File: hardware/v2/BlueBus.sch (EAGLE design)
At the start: 139 parts, among them J1 3PIN_953442_1, J2 6PIN_953442_1, J3 6PIN_5_103166_1, J4 SJ2-35853A-SMT-TR, J5 SMB_CONN, J6 USB3080-30-01-A, J7 PCM12SMTR, J8 TC2030NL, Q1 NMOSFET-BSS138K, Q2 NMOSFET-BSS138K, Q3 PMOSFET-DMP32D4SSOT323, U1 MPQ4420, U10 PCM5122, U11 PAM8406, U2 TH3122.4, U3 FT231XS, U4 S-1212BC0-U5T1U, U5 XC6210, U6 CAT25M01, U7 PIC24FJ1024GA606, U8 BM83SM1, U9 DIT4096

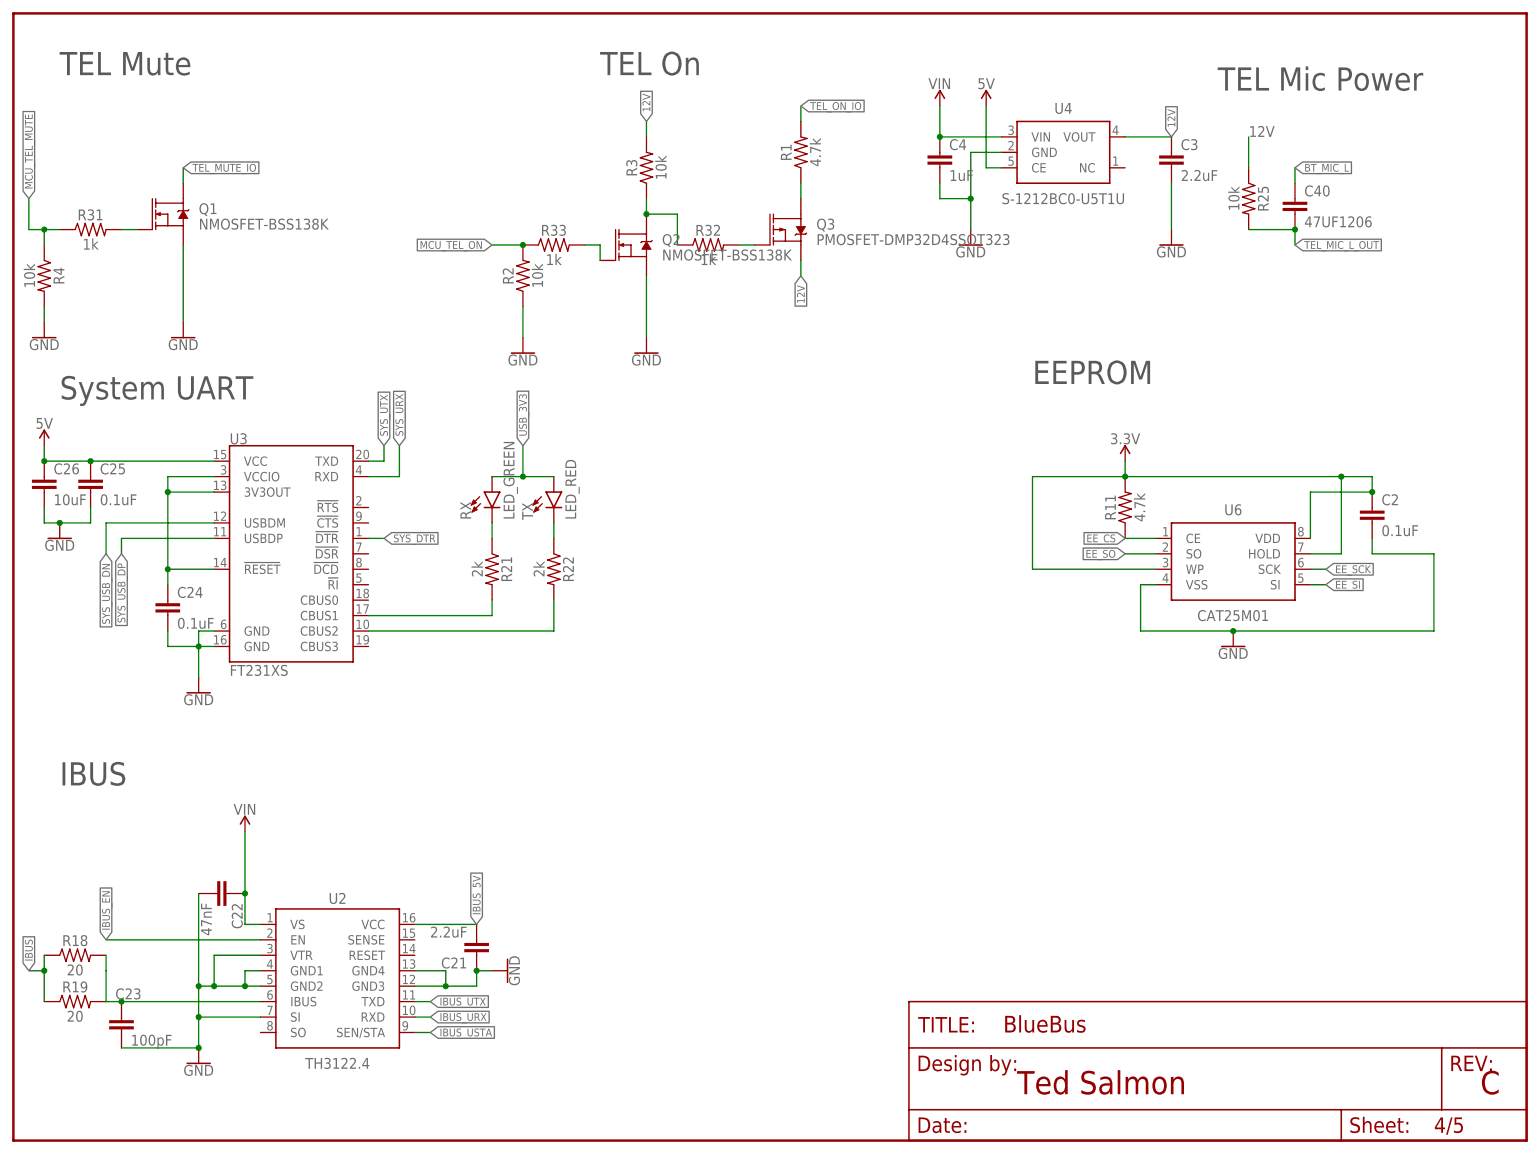
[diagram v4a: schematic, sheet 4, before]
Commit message: [IMP] hardware: v2.0 Silkscreen * Update Bottom Silkscreen * Renumber Resistors
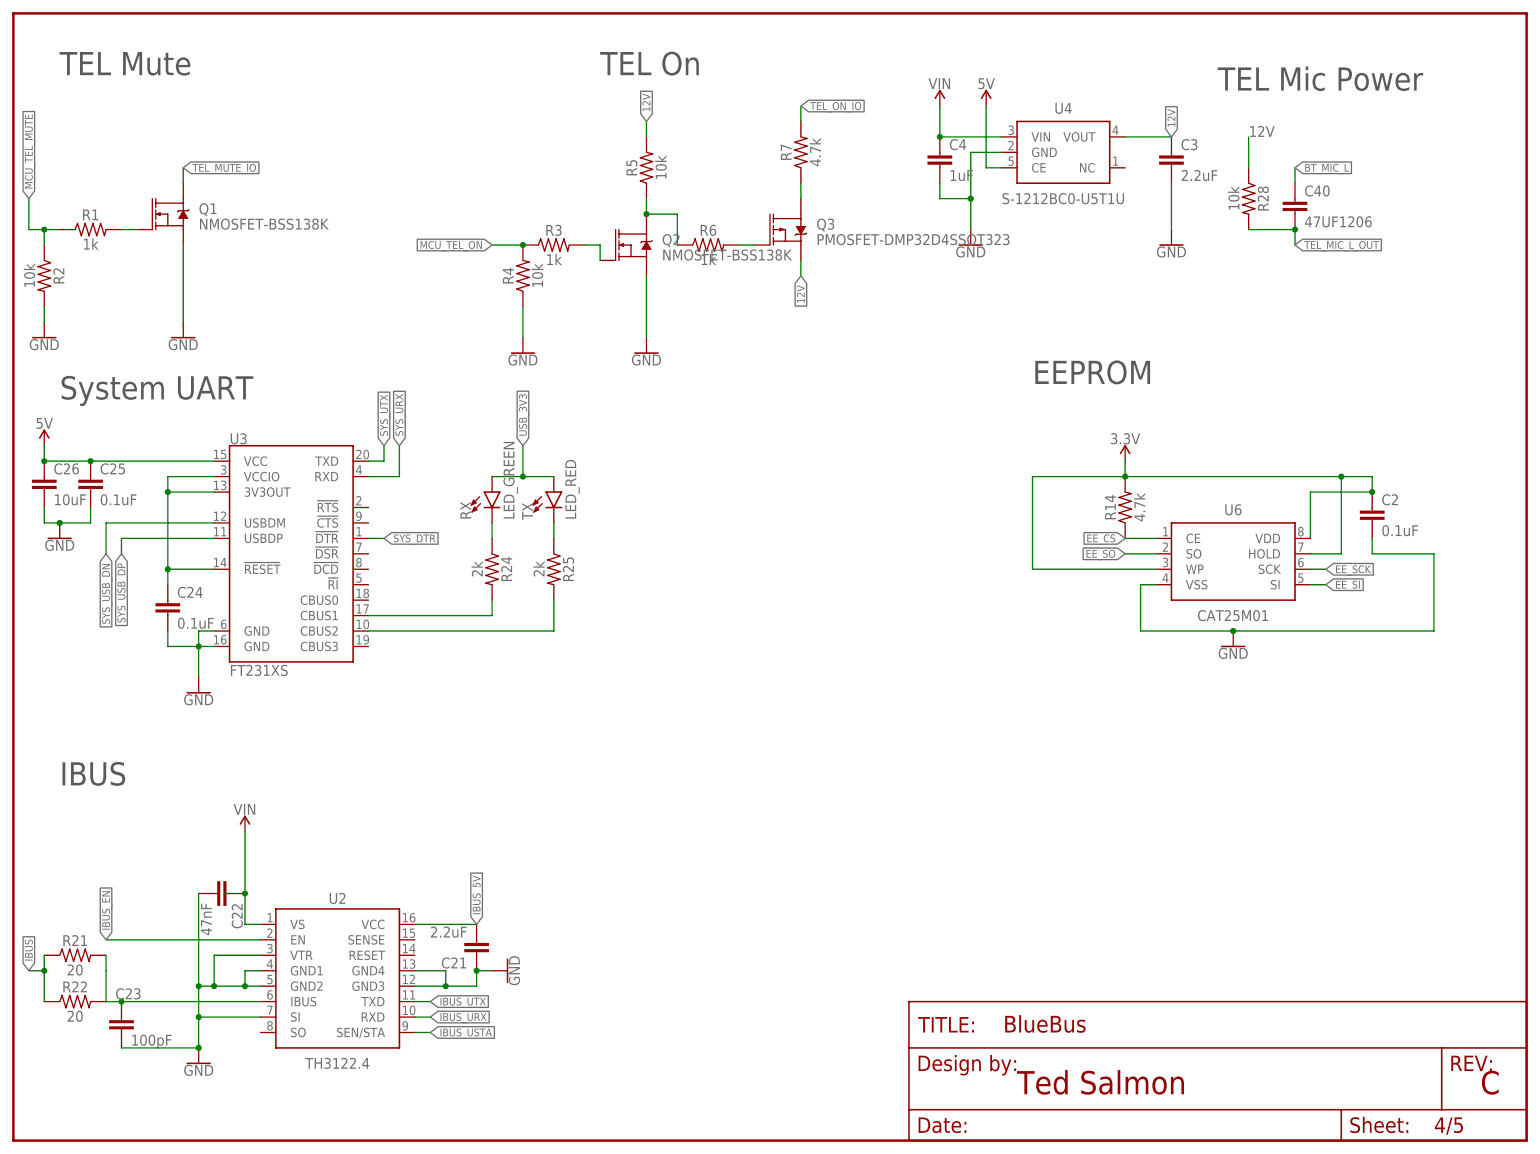
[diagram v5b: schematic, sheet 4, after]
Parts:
- R1: value 4.7k -> 1k; device Passives:4.7KOHM0603 -> Passives:1KOHM0603
- R10: value 100k -> 41.2k; device Passives:100KOHM0603 -> Passives:41.2KOHM0603
- R11: value 4.7k -> 7.68k; device Passives:4.7KOHM0603 -> Passives:7.68KOHM0603
- R12: value 4.7k -> 51k; device Passives:4.7KOHM0603 -> Passives:51KOHM0603
- R13: value 4.7k -> 100k; device Passives:4.7KOHM0603 -> Passives:100KOHM0603
- R14, R16: value 10k -> 4.7k; device Passives:10KOHM0603 -> Passives:4.7KOHM0603
- R15: value 150 -> 4.7k; device Passives:150OHM0603 -> Passives:4.7KOHM0603
- R18: value 20 -> 150; device Passives:20OHM0603 -> Passives:150OHM0603
- R19, R5: value 20 -> 10k; device Passives:20OHM0603 -> Passives:10KOHM0603
- R20: value 2k -> 10k; device Passives:2KOHM0603 -> Passives:10KOHM0603
- R21, R22: value 2k -> 20; device Passives:2KOHM0603 -> Passives:20OHM0603
- R23, R24: value 1k -> 2k; device Passives:1KOHM0603 -> Passives:2KOHM0603
- R25: value 10k -> 2k; device Passives:10KOHM0603 -> Passives:2KOHM0603
- R26: value 18k -> 1k; device Passives:18KOHM0603 -> Passives:1KOHM0603
- R27: value 150 -> 1k; device Passives:150OHM0603 -> Passives:1KOHM0603
- R28: value 150 -> 10k; device Passives:150OHM0603 -> Passives:10KOHM0603
- R29: value 100 -> 18k; device Passives:100OHM0603 -> Passives:18KOHM0603
- R3: value 10k -> 1k; device Passives:10KOHM0603 -> Passives:1KOHM0603
- R30: value 100 -> 150; device Passives:100OHM0603 -> Passives:150OHM0603
- R31: value 1k -> 150; device Passives:1KOHM0603 -> Passives:150OHM0603
- R32, R33: value 1k -> 100; device Passives:1KOHM0603 -> Passives:100OHM0603
- R6: value 100k -> 1k; device Passives:100KOHM0603 -> Passives:1KOHM0603
- R7: value 41.2k -> 4.7k; device Passives:41.2KOHM0603 -> Passives:4.7KOHM0603
- R8: value 7.68k -> 20; device Passives:7.68KOHM0603 -> Passives:20OHM0603
- R9: value 51k -> 100k; device Passives:51KOHM0603 -> Passives:100KOHM0603
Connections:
- net 12V: now also R28.1, R5.2; no longer R25.1, R3.2
- net 3.3V: now also R14.2, R15.2, R17.1, R19.2, R20.2; no longer R11.2, R12.2, R13.2, R14.1, R17.2
- net 5V: now also R10.2; no longer R7.2
- net 5VREG_BS: now also R8.1; no longer R5.1
- net 5VREG_BS_CAP: now also R8.2; no longer R5.2
- net 5VREG_EN: now also R9.1; no longer R6.1
- net 5VREG_FB: now also R12.2; no longer R9.2
- net 5VREG_FB_T: now also R10.1, R11.2, R12.1; no longer R7.1, R8.2, R9.1
- net 5VREG_PG: now also R13.1; no longer R10.1
- net 5VREG_VCC: now also R13.2; no longer R10.2
- net BT_MIC_L: now also R26.1; no longer R23.1
- net DAC_OUT_L: now also R32.1; no longer R29.1
- net DAC_OUT_R: now also R33.1; no longer R30.1
- net EE_CS: now also R14.1; no longer R11.1
- net GND: now also R11.1, R2.2, R30.2, R4.1; no longer R2.1, R27.2, R4.2, R8.1
- net IBUS: now also R21.1, R22.1; no longer R18.1, R19.1
- net IBUS_5V: now also R9.2; no longer R6.2
- net IBUS_FILT: now also R21.2, R22.2; no longer R18.2, R19.2
- net MCU_MCLR: now also R18.2; no longer R15.2
- net MCU_MCLR_RES: now also R17.2, R18.1; no longer R14.2, R15.1
- net MCU_ON_LED: now also R23.2; no longer R20.2
- net MCU_ON_LED_RES: now also R23.1; no longer R20.1
- net MCU_SCK3: now also R16.1; no longer R13.1
- net MCU_SDA3: now also R15.1; no longer R12.1
- net MCU_TEL_MUTE: now also R1.1, R2.1; no longer R31.1, R4.1
- net MCU_TEL_MUTE_RES: now also R1.2; no longer R31.2
- net MCU_TEL_ON: now also R3.1, R4.2; no longer R2.2, R33.1
- net MCU_TEL_ON_NRES: now also R3.2; no longer R33.2
- net MCU_VER: now also R19.1; no longer R16.1
- net MICP1_RES: now also R26.2, R27.1; no longer R23.2, R24.1
- net MIC_BIAS: now also R27.2; no longer R24.2
- net RECOVERY_ON: now also R20.1; no longer R17.1
- net SPDIF_OUT: now also R30.1, R31.2; no longer R27.1, R28.2
- net SPDIF_TX_RES: now also R31.1; no longer R28.1
- net SPKR_OUT_L: now also R32.2; no longer R29.2
- net SPKR_OUT_R: now also R33.2; no longer R30.2
- net SYS_RX_LED: now also R24.2; no longer R21.2
- net SYS_RX_LED_RES: now also R24.1; no longer R21.1
- net SYS_TX_LED: now also R25.2; no longer R22.2
- net SYS_TX_LED_RES: now also R25.1; no longer R22.1
- net TEL_AMP_INL: now also R29.2; no longer R26.2
- net TEL_AMP_INL_CAP_RES: now also R29.1; no longer R26.1
- net TEL_MIC_L_OUT: now also R28.2; no longer R25.2
- net TEL_ON: now also R7.1; no longer R1.1
- net TEL_ON_IO: now also R7.2; no longer R1.2
- net TEL_ON_P: now also R5.1, R6.1; no longer R3.1, R32.1
- net TEL_ON_P_RES: now also R6.2; no longer R32.2
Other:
- moved on the sheet: R1, R10, R15, R16, R2, R21, R22, R25, R29, R3, R30, R4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
